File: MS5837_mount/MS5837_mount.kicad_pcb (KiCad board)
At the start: 2 copper layers, 11.5 x 13 mm, 3 parts, among them P1 CONN_01X04, U1 MS5837-30BA

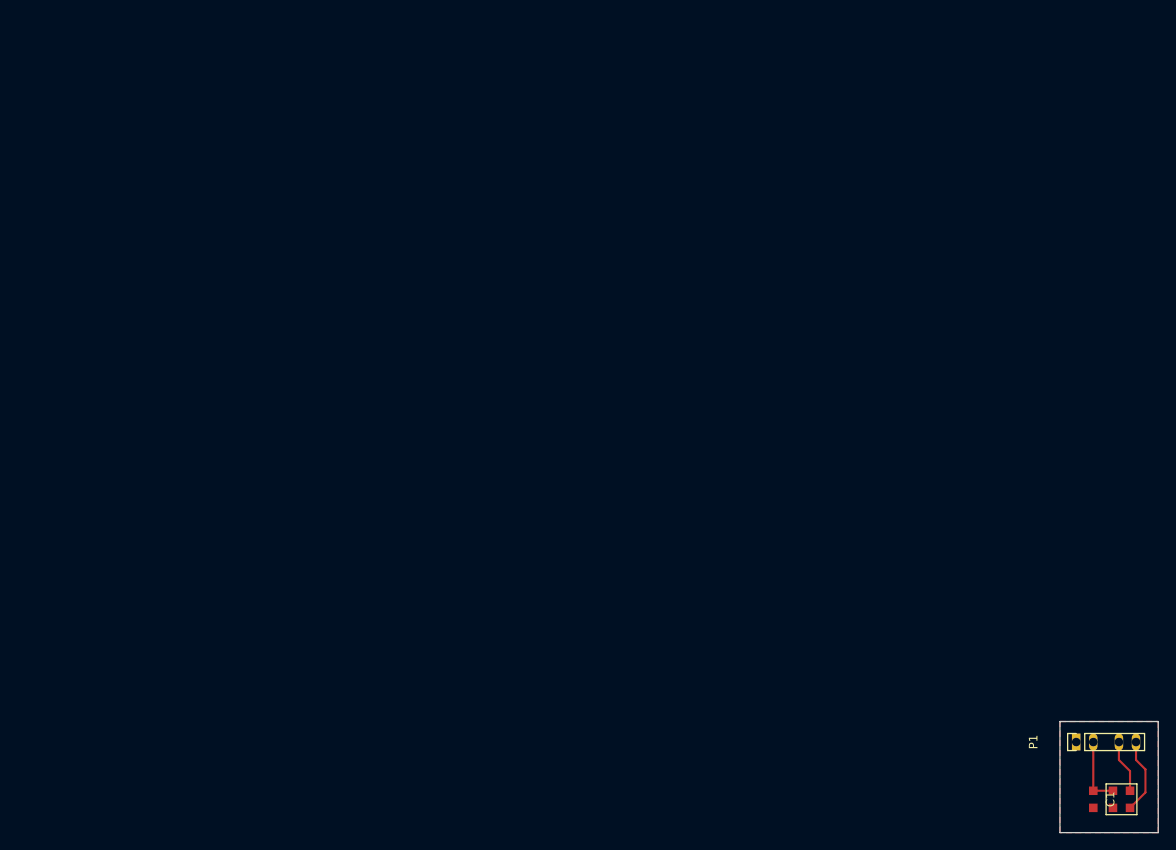
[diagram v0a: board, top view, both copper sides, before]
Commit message: Make pcb round
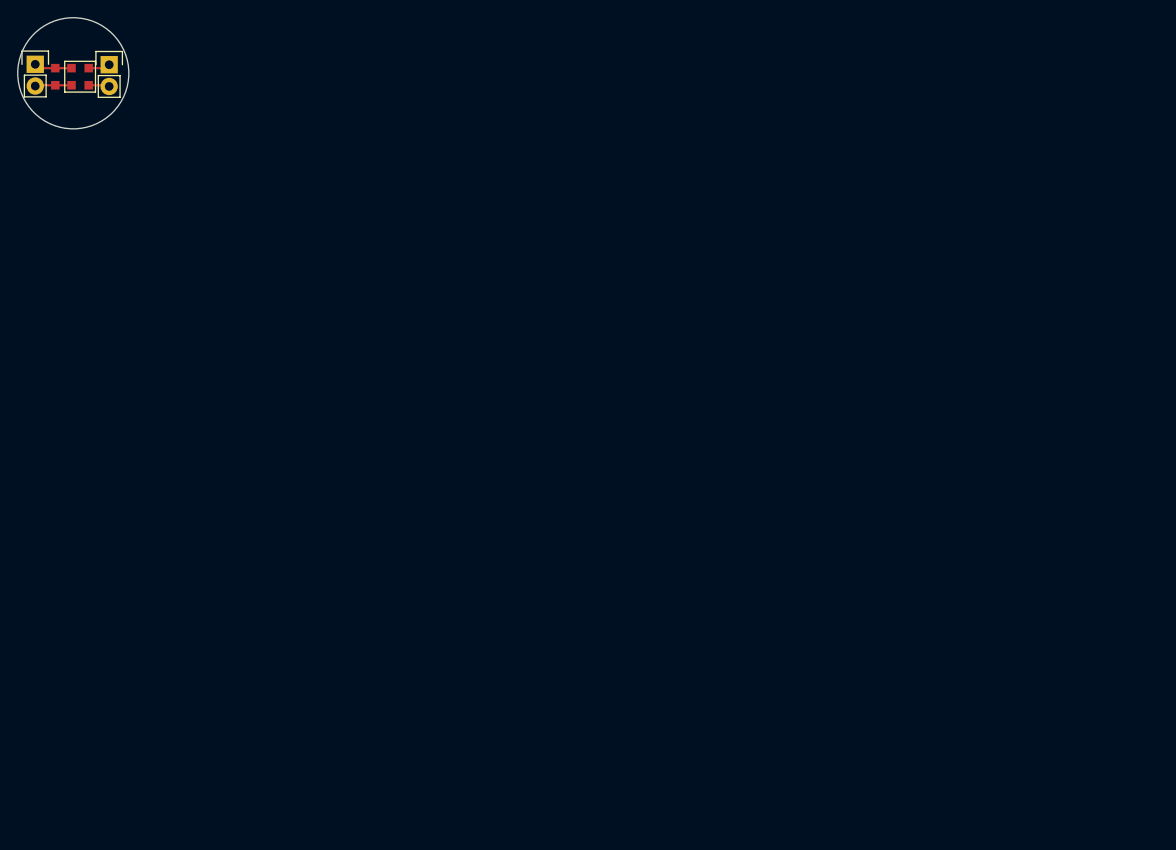
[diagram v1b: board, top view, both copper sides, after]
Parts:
- added P2: CONN_01X02, Pin_Headers:Pin_Header_Straight_1x02, F.Cu at (36.2, 30.1)
- P1: value CONN_01X04 -> CONN_01X02; footprint Pin_Headers:Pin_Header_Straight_1x04 -> Pin_Headers:Pin_Header_Straight_1x02
- U1: value MS5837-30BA -> MS5837
- moved U1 148.3 mm to (32.9, 31.6)
- moved C1 148.0 mm to (29.9, 31.6)
- moved P1 145.3 mm to (27.6, 30.1), turned to 0 degrees
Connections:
- P1 pad 1: GND -> VCC
- P1 pad 2: VCC -> GND
- U1 pad 3: Net-(P1-Pad3) -> Net-(P2-Pad1)
- U1 pad 4: Net-(P1-Pad4) -> Net-(P2-Pad2)
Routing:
- net Net-(P1-Pad4): track 8.90 -> 0.00 mm
- net Net-(P1-Pad3): track 6.24 -> 0.00 mm
- net GND: track 0.00 -> 4.16 mm
- net VCC: track 8.00 -> 5.07 mm
- net Net-(P2-Pad1): track 0.00 -> 2.57 mm
- net Net-(P2-Pad2): track 0.00 -> 2.46 mm
- removed copper zone on F.Cu, net GND
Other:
- board size 11.5 x 13 mm -> 13 x 13 mm
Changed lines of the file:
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@@
     (links 6)
     (no_connects 0)
-    (area 147.924999 106.924999 159.075001 120.075001)
+    (area 25.474999 24.574999 38.625001 37.725001)
     (thickness 1.6)
-    (drawings 4)
-    (tracks 9)
+    (drawings 1)
+    (tracks 10)
     (zones 0)
-    (modules 3)
+    (modules 4)
     (nets 5)
   )
@@
     (35 F.Paste user)
     (36 B.SilkS user)
-    (37 F.SilkS user)
+    (37 F.SilkS user hide)
     (38 B.Mask user)
     (39 F.Mask user)
@@
     (45 Margin user)
     (46 B.CrtYd user)
-    (47 F.CrtYd user)
+    (47 F.CrtYd user hide)
     (48 B.Fab user)
     (49 F.Fab user)
@@
   (net 1 VCC)
   (net 2 GND)
-  (net 3 "Net-(P1-Pad3)")
-  (net 4 "Net-(P1-Pad4)")
+  (net 3 "Net-(P2-Pad1)")
+  (net 4 "Net-(P2-Pad2)")
   (net_class Default "This is the default net class."
     (clearance 0.25)
@@
     (uvia_drill 0.1)
     (add_net GND)
-    (add_net "Net-(P1-Pad3)")
-    (add_net "Net-(P1-Pad4)")
+    (add_net "Net-(P2-Pad1)")
+    (add_net "Net-(P2-Pad2)")
     (add_net VCC)
   )
+  (module Pin_Headers:Pin_Header_Straight_1x02 (layer F.Cu)
+    (at 27.6 30.1)
+    (descr "Through hole pin header")
+    (tags "pin header")
+    (fp_text reference P1 (at 0 -2.4) (layer F.SilkS) hide
+      (effects (font (size 1 1) (thickness 0.15)))
+    )
+    (fp_text value CONN_01X02 (at -7.2 1.2) (layer F.Fab) hide
+      (effects (font (size 1 1) (thickness 0.15)))
+    )
+    (fp_line (start 1.27 1.27) (end 1.27 3.81) (layer F.SilkS) (width 0.15))
+    (fp_line (start 1.55 -1.55) (end 1.55 0) (layer F.SilkS) (width 0.15))
+    (fp_line (start -1.75 -1.75) (end -1.75 4.3) (layer F.CrtYd) (width 0.05))
+    (fp_line (start 1.75 -1.75) (end 1.75 4.3) (layer F.CrtYd) (width 0.05))
+    (fp_line (start -1.75 -1.75) (end 1.75 -1.75) (layer F.CrtYd) (width 0.05))
+    (fp_line (start -1.75 4.3) (end 1.75 4.3) (layer F.CrtYd) (width 0.05))
+    (fp_line (start 1.27 1.27) (end -1.27 1.27) (layer F.SilkS) (width 0.15))
+    (fp_line (start -1.55 0) (end -1.55 -1.55) (layer F.SilkS) (width 0.15))
+    (fp_line (start -1.55 -1.55) (end 1.55 -1.55) (layer F.SilkS) (width 0.15))
+    (fp_line (start -1.27 1.27) (end -1.27 3.81) (layer F.SilkS) (width 0.15))
+    (fp_line (start -1.27 3.81) (end 1.27 3.81) (layer F.SilkS) (width 0.15))
+    (pad 1 thru_hole rect (at 0 0) (size 2.032 2.032) (drill 1.016) (layers *.Cu *.Mask F.SilkS)
+      (net 1 VCC))
+    (pad 2 thru_hole oval (at 0 2.54) (size 2.032 2.032) (drill 1.016) (layers *.Cu *.Mask F.SilkS)
+      (net 2 GND))
+    (model Pin_Headers.3dshapes/Pin_Header_Straight_1x02.wrl
+      (at (xyz 0 -0.05 0))
+      (scale (xyz 1 1 1))
+      (rotate (xyz 0 0 90))
+    )
+  )
   (module Capacitors_SMD:C_0805_HandSoldering (layer F.Cu)
-    (at 151.4 116.1 270)
+    (at 29.95 31.55 270)
     (descr "Capacitor SMD 0805, hand soldering")
     (tags "capacitor 0805")
     (attr smd)
-    (fp_text reference C1 (at 0 -2 270) (layer F.SilkS)
-      (effects (font (size 1 1)))
-    )
-    (fp_text value C (at 0 2 270) (layer F.Fab)
-      (effects (font (size 1 1)))
+    (fp_text reference C1 (at 2.85 -0.05 360) (layer F.SilkS) hide
+      (effects (font (size 1 1) (thickness 0.15)))
+    )
+    (fp_text value C (at 2.65 0.15 360) (layer F.Fab)
+      (effects (font (size 1 1) (thickness 0.15)))
     )
     (fp_line (start -2 -1) (end 2 -1) (layer F.CrtYd) (width 0))
@@
     )
   )
-  (module Pin_Headers:Pin_Header_Straight_1x04 (layer F.Cu)
-    (at 149.4 109.4 90)
-    (descr "Through hole pin header")
-    (tags "pin header")
-    (fp_text reference P1 (at 0 -5 90) (layer F.SilkS)
-      (effects (font (size 1 1)))
-    )
-    (fp_text value CONN_01X04 (at 0 -3 90) (layer F.Fab)
-      (effects (font (size 1 1)))
-    )
-    (fp_line (start -1 -1) (end -1 9) (layer F.CrtYd) (width 0))
-    (fp_line (start 1 -1) (end 1 9) (layer F.CrtYd) (width 0))
-    (fp_line (start -1 -1) (end 1 -1) (layer F.CrtYd) (width 0))
-    (fp_line (start -1 9) (end 1 9) (layer F.CrtYd) (width 0))
-    (fp_line (start -1 1) (end -1 8) (layer F.SilkS) (width 0))
-    (fp_line (start 1 1) (end 1 8) (layer F.SilkS) (width 0))
-    (fp_line (start 1 -1) (end 1 0) (layer F.SilkS) (width 0))
-    (fp_line (start -1 8) (end 1 8) (layer F.SilkS) (width 0))
-    (fp_line (start 1 1) (end -1 1) (layer F.SilkS) (width 0))
-    (fp_line (start -1 0) (end -1 -1) (layer F.SilkS) (width 0))
-    (fp_line (start -1 -1) (end 1 -1) (layer F.SilkS) (width 0))
-    (pad 1 thru_hole rect (at 0 0 90) (size 2 1) (drill 1) (layers *.Cu *.Mask F.SilkS)
-      (net 2 GND))
-    (pad 2 thru_hole oval (at 0 2 90) (size 2 1) (drill 1) (layers *.Cu *.Mask F.SilkS)
-      (net 1 VCC))
-    (pad 3 thru_hole oval (at 0 5 90) (size 2 1) (drill 1) (layers *.Cu *.Mask F.SilkS)
-      (net 3 "Net-(P1-Pad3)"))
-    (pad 4 thru_hole oval (at 0 7 90) (size 2 1) (drill 1) (layers *.Cu *.Mask F.SilkS)
-      (net 4 "Net-(P1-Pad4)"))
-    (model Pin_Headers.3dshapes/Pin_Header_Straight_1x04.wrl
-      (at (xyz 0 -0 0))
-      (scale (xyz 1 1 1))
-      (rotate (xyz 0 0 90))
-    )
-  )
   (module MS5837:MS5837-BA30 (layer F.Cu)
-    (at 154.7 116.1)
+    (at 32.85 31.55)
     (fp_text reference U1 (at 0 3) (layer F.SilkS) hide
       (effects (font (size 1 1) (thickness 0.15)))
     )
-    (fp_text value MS5837-30BA (at -1.5 2.9) (layer F.Fab)
+    (fp_text value MS5837 (at -0.95 -2.95) (layer F.Fab)
       (effects (font (size 1 1) (thickness 0.15)))
     )
@@
       (net 1 VCC))
     (pad 3 smd rect (at 1 -1) (size 1 1) (layers F.Cu F.Paste F.Mask)
-      (net 3 "Net-(P1-Pad3)"))
+      (net 3 "Net-(P2-Pad1)"))
     (pad 1 smd rect (at -1 1) (size 1 1) (layers F.Cu F.Paste F.Mask)
       (net 2 GND))
     (pad 4 smd rect (at 1 1) (size 1 1) (layers F.Cu F.Paste F.Mask)
-      (net 4 "Net-(P1-Pad4)"))
-  )
-  (gr_line (start 159 107) (end 147.5 107) (angle 90) (layer Edge.Cuts) (width 0.15))
-  (gr_line (start 159 120) (end 159 107) (angle 90) (layer Edge.Cuts) (width 0.15))
-  (gr_line (start 147.5 120) (end 159 120) (angle 90) (layer Edge.Cuts) (width 0.15))
-  (gr_line (start 147.5 107) (end 147.5 120) (angle 90) (layer Edge.Cuts) (width 0.15))
-  (segment (start 151.4 115.1) (end 153.7 115.1) (width 0.25) (layer F.Cu) (net 1))
-  (segment (start 151.4 109.4) (end 151.4 115.1) (width 0.25) (layer F.Cu) (net 1))
-  (segment (start 154.4 109.4) (end 154.4 111.5) (width 0.25) (layer F.Cu) (net 3))
-  (segment (start 155.7 112.8) (end 155.7 115.1) (width 0.25) (layer F.Cu) (net 3))
-  (segment (start 154.4 111.5) (end 155.7 112.8) (width 0.25) (layer F.Cu) (net 3))
-  (segment (start 156.4 109.4) (end 156.4 111.5) (width 0.25) (layer F.Cu) (net 4))
-  (segment (start 157.5 115.3) (end 155.7 117.1) (width 0.25) (layer F.Cu) (net 4))
-  (segment (start 157.5 112.6) (end 157.5 115.3) (width 0.25) (layer F.Cu) (net 4))
-  (segment (start 156.4 111.5) (end 157.5 112.6) (width 0.25) (layer F.Cu) (net 4))
-  (zone (net 2) (net_name GND) (layer F.Cu) (hatch edge 0.508)
-    (connect_pads (clearance 0.5))
-    (min_thickness 0.1)
-    (fill yes (arc_segments 16) (thermal_gap 0.5) (thermal_bridge_width 0.5))
-    (polygon
-      (pts
-        (xy 159 120) (xy 147.5 120) (xy 147.5 107) (xy 159 107) (xy 159 120)
-      )
-    )
-  )
+      (net 4 "Net-(P2-Pad2)"))
+  )
+  (module Pin_Headers:Pin_Header_Straight_1x02 (layer F.Cu)
+    (at 36.25 30.15)
+    (descr "Through hole pin header")
+    (tags "pin header")
+    (fp_text reference P2 (at -0.05 -2.55) (layer F.SilkS) hide
+      (effects (font (size 1 1) (thickness 0.15)))
+    )
+    (fp_text value CONN_01X02 (at 7.25 1.05) (layer F.Fab) hide
+      (effects (font (size 1 1) (thickness 0.15)))
+    )
+    (fp_line (start 1.27 1.27) (end 1.27 3.81) (layer F.SilkS) (width 0.15))
+    (fp_line (start 1.55 -1.55) (end 1.55 0) (layer F.SilkS) (width 0.15))
+    (fp_line (start -1.75 -1.75) (end -1.75 4.3) (layer F.CrtYd) (width 0.05))
+    (fp_line (start 1.75 -1.75) (end 1.75 4.3) (layer F.CrtYd) (width 0.05))
+    (fp_line (start -1.75 -1.75) (end 1.75 -1.75) (layer F.CrtYd) (width 0.05))
+    (fp_line (start -1.75 4.3) (end 1.75 4.3) (layer F.CrtYd) (width 0.05))
+    (fp_line (start 1.27 1.27) (end -1.27 1.27) (layer F.SilkS) (width 0.15))
+    (fp_line (start -1.55 0) (end -1.55 -1.55) (layer F.SilkS) (width 0.15))
+    (fp_line (start -1.55 -1.55) (end 1.55 -1.55) (layer F.SilkS) (width 0.15))
+    (fp_line (start -1.27 1.27) (end -1.27 3.81) (layer F.SilkS) (width 0.15))
+    (fp_line (start -1.27 3.81) (end 1.27 3.81) (layer F.SilkS) (width 0.15))
+    (pad 1 thru_hole rect (at 0 0) (size 2.032 2.032) (drill 1.016) (layers *.Cu *.Mask F.SilkS)
+      (net 3 "Net-(P2-Pad1)"))
+    (pad 2 thru_hole oval (at 0 2.54) (size 2.032 2.032) (drill 1.016) (layers *.Cu *.Mask F.SilkS)
+      (net 4 "Net-(P2-Pad2)"))
+    (model Pin_Headers.3dshapes/Pin_Header_Straight_1x02.wrl
+      (at (xyz 0 -0.05 0))
+      (scale (xyz 1 1 1))
+      (rotate (xyz 0 0 90))
+    )
+  )
+  (gr_circle (center 32.05 31.15) (end 32.05 24.65) (layer Edge.Cuts) (width 0.15))
+  (segment (start 29.95 30.55) (end 28.05 30.55) (width 0.25) (layer F.Cu) (net 1))
+  (segment (start 28.05 30.55) (end 27.6 30.1) (width 0.25) (layer F.Cu) (net 1))
+  (segment (start 28.05 30.55) (end 27.6 30.1) (width 0.25) (layer F.Cu) (net 1))
+  (segment (start 29.95 30.55) (end 31.85 30.55) (width 0.25) (layer F.Cu) (net 1))
+  (segment (start 29.95 32.55) (end 27.69 32.55) (width 0.25) (layer F.Cu) (net 2))
+  (segment (start 31.85 32.55) (end 29.95 32.55) (width 0.25) (layer F.Cu) (net 2))
+  (segment (start 33.85 30.55) (end 35.85 30.55) (width 0.25) (layer F.Cu) (net 3))
+  (segment (start 35.85 30.55) (end 36.25 30.15) (width 0.25) (layer F.Cu) (net 3))
+  (segment (start 33.85 32.55) (end 36.11 32.55) (width 0.25) (layer F.Cu) (net 4))
+  (segment (start 36.11 32.55) (end 36.25 32.69) (width 0.25) (layer F.Cu) (net 4))
 )
